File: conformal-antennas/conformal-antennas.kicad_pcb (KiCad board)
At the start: 2 copper layers, 153.9 x 117.1 mm, 1 part, among them J1 Conn_Coaxial

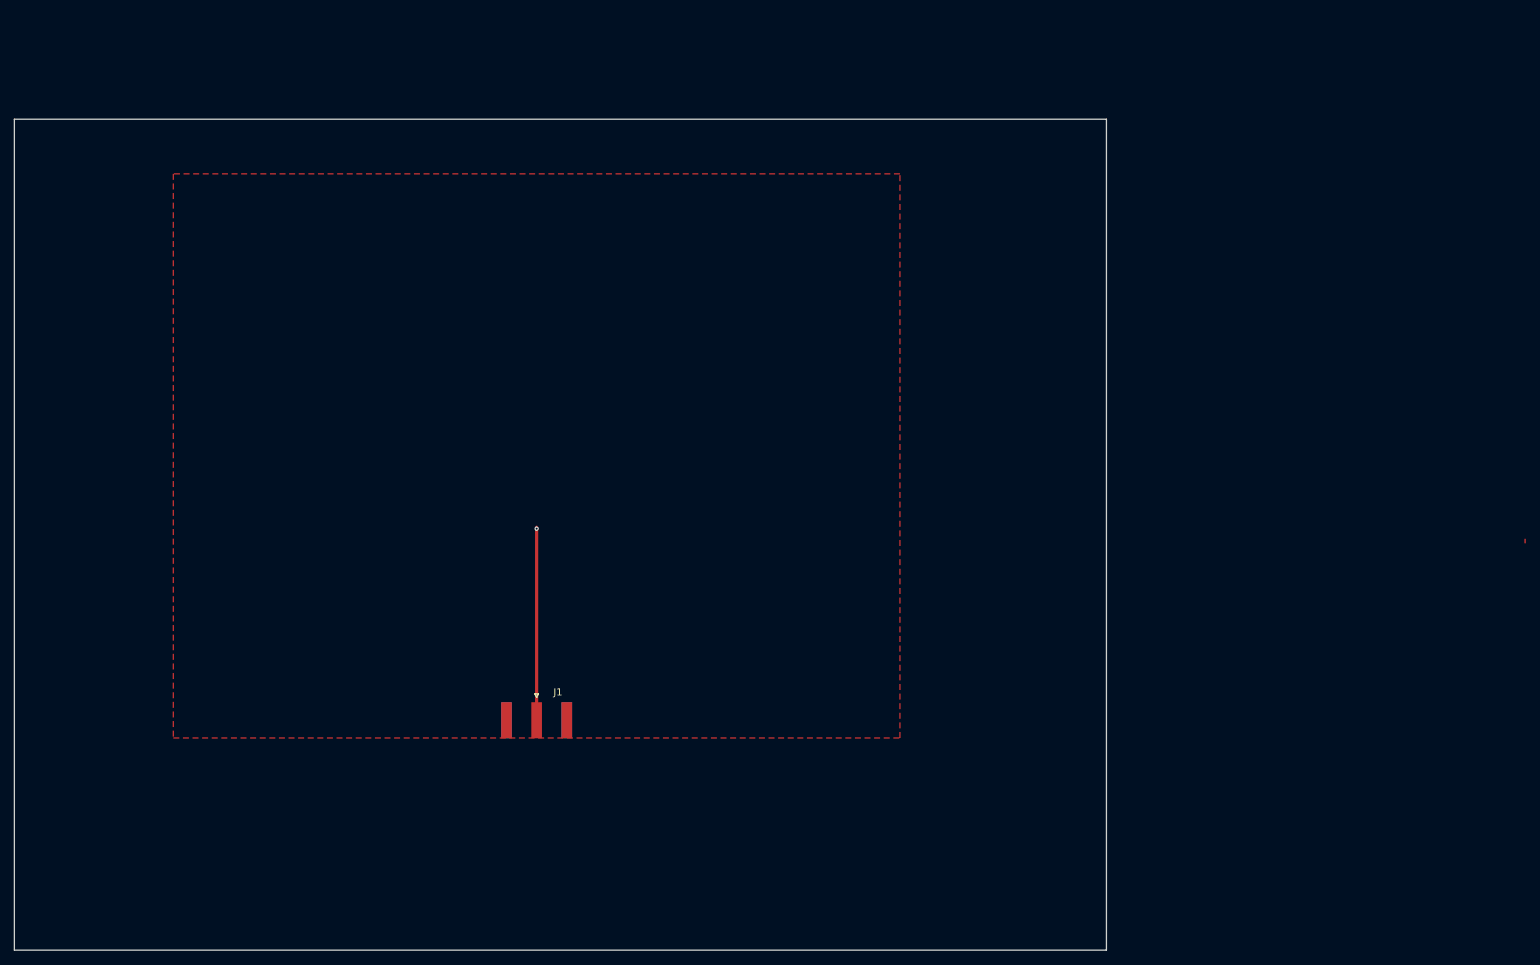
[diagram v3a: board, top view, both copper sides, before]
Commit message: Resized signal trace and added ground plane
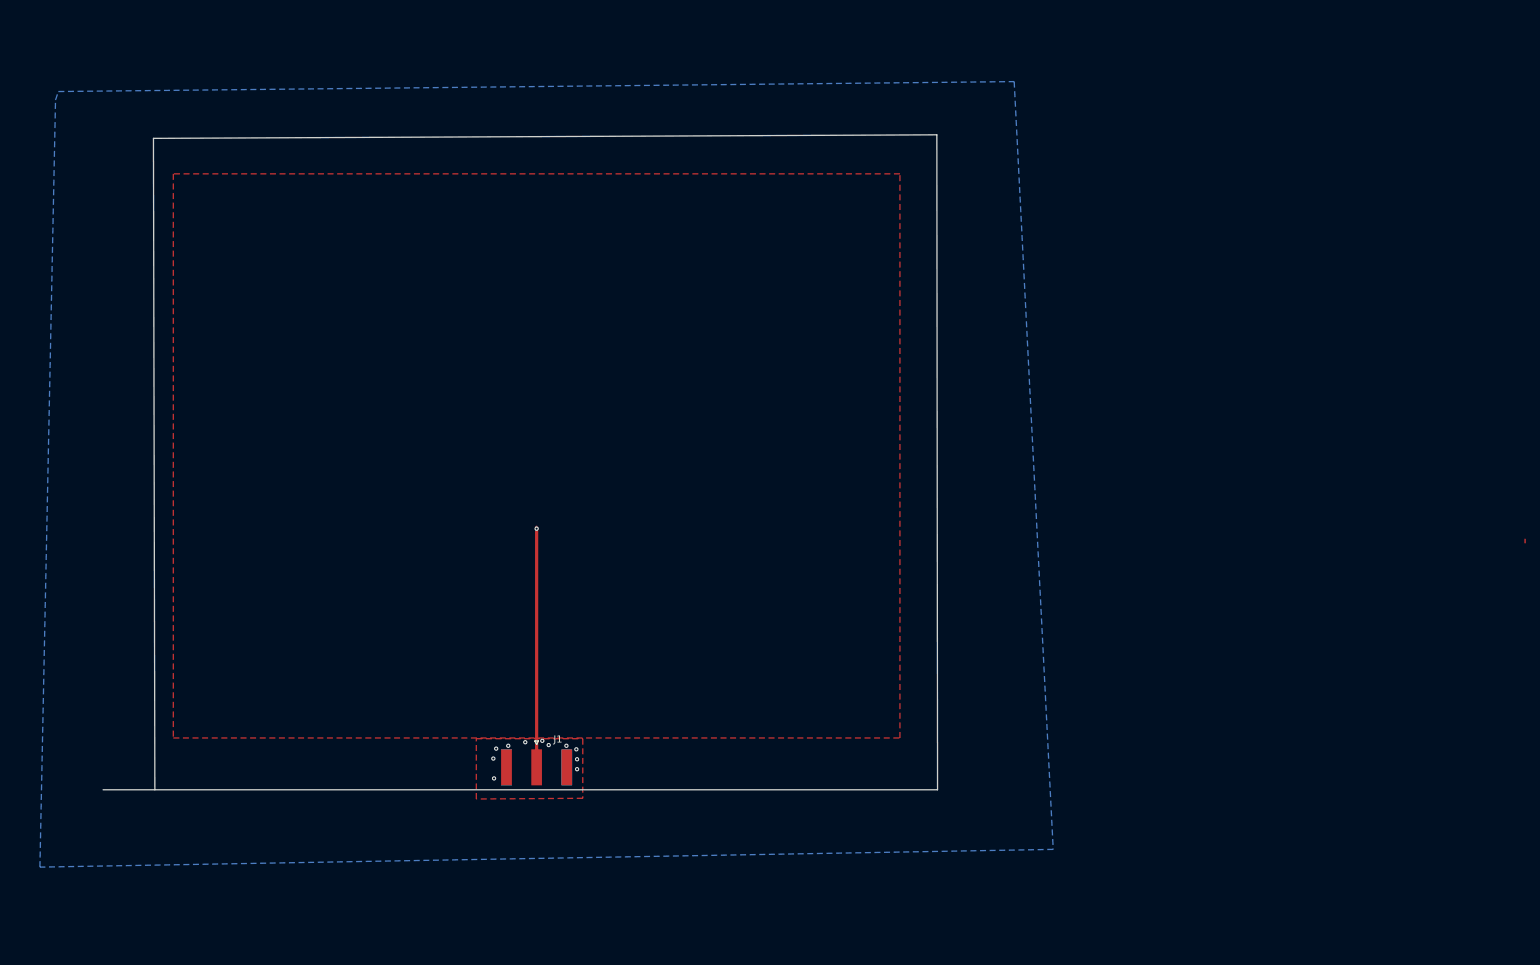
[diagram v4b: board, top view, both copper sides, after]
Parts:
- moved J1 6.64 mm to (108.2, 150.6)
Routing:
- net /Signal: track 27.2 -> 32.1 mm
- net GND: vias 0 -> 11
- added copper zone on B.Cu, net GND
- added copper zone on F.Cu, net GND
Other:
- board size 153.9 x 117.1 mm -> 117.6 x 92.3 mm
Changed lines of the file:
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@@
 	(footprint "Connector_Coaxial:SMA_Amphenol_132289_EdgeMount"
 		(layer "F.Cu")
-		(at 108.2 144 -90)
+		(at 108.2 150.6375 -90)
 		(descr "https://www.amphenolrf.com/library/download/link/link_id/595984/parent/132289/")
 		(tags "SMA")
@@
 		)
 	)
-	(gr_rect
-		(start 34.6 59.3)
-		(end 188.5 176.4)
+	(gr_line
+		(start 164.6 61.5)
+		(end 164.7 153.8)
 		(stroke
 			(width 0.05)
 			(type default)
 		)
-		(fill no)
+		(layer "Edge.Cuts")
+	)
+	(gr_line
+		(start 54.4 153.8)
+		(end 54.2 62)
+		(stroke
+			(width 0.05)
+			(type default)
+		)
+		(layer "Edge.Cuts")
+	)
+	(gr_line
+		(start 54.2 62)
+		(end 164.6 61.5)
+		(stroke
+			(width 0.05)
+			(type default)
+		)
+		(layer "Edge.Cuts")
+	)
+	(gr_line
+		(start 164.7 153.8)
+		(end 47.1 153.8)
+		(stroke
+			(width 0.05)
+			(type default)
+		)
 		(layer "Edge.Cuts")
 	)
@@
 		(net 0)
 	)
+	(via
+		(at 102.1 149.4)
+		(size 0.6)
+		(drill 0.3)
+		(layers "F.Cu" "B.Cu")
+		(free yes)
+		(net 1)
+	)
+	(via
+		(at 112.4 147.6)
+		(size 0.6)
+		(drill 0.3)
+		(layers "F.Cu" "B.Cu")
+		(free yes)
+		(net 1)
+	)
+	(via
+		(at 113.9 150.9)
+		(size 0.6)
+		(drill 0.3)
+		(layers "F.Cu" "B.Cu")
+		(free yes)
+		(net 1)
+	)
+	(via
+		(at 106.6 147.1)
+		(size 0.6)
+		(drill 0.3)
+		(layers "F.Cu" "B.Cu")
+		(free yes)
+		(net 1)
+	)
+	(via
+		(at 104.2 147.6)
+		(size 0.6)
+		(drill 0.3)
+		(layers "F.Cu" "B.Cu")
+		(free yes)
+		(net 1)
+	)
+	(via
+		(at 113.9 149.5)
+		(size 0.6)
+		(drill 0.3)
+		(layers "F.Cu" "B.Cu")
+		(free yes)
+		(net 1)
+	)
+	(via
+		(at 102.2 152.2)
+		(size 0.6)
+		(drill 0.3)
+		(layers "F.Cu" "B.Cu")
+		(free yes)
+		(net 1)
+	)
+	(via
+		(at 113.8 148.1)
+		(size 0.6)
+		(drill 0.3)
+		(layers "F.Cu" "B.Cu")
+		(free yes)
+		(net 1)
+	)
+	(via
+		(at 109 146.9)
+		(size 0.6)
+		(drill 0.3)
+		(layers "F.Cu" "B.Cu")
+		(free yes)
+		(net 1)
+	)
+	(via
+		(at 109.9 147.5)
+		(size 0.6)
+		(drill 0.3)
+		(layers "F.Cu" "B.Cu")
+		(free yes)
+		(net 1)
+	)
+	(via
+		(at 102.5 148)
+		(size 0.6)
+		(drill 0.3)
+		(layers "F.Cu" "B.Cu")
+		(free yes)
+		(net 1)
+	)
 	(segment
-		(start 108.2 144)
-		(end 108.2 117)
+		(start 108.2 117)
+		(end 108.2 148.874)
 		(width 0.45)
 		(layer "F.Cu")
@@
 			)
 		)
+	)
+	(zone
+		(net 1)
+		(net_name "GND")
+		(layer "F.Cu")
+		(hatch edge 0.5)
+		(priority 2)
+		(connect_pads yes
+			(clearance 0.5)
+		)
+		(min_thickness 0.25)
+		(filled_areas_thickness no)
+		(fill yes
+			(thermal_gap 0.5)
+			(thermal_bridge_width 0.5)
+		)
+		(polygon
+			(pts
+				(xy 114.7 146.6) (xy 114.7 155) (xy 99.7 155.1) (xy 99.7 146.6)
+			)
+		)
+	)
+	(zone
+		(net 1)
+		(net_name "GND")
+		(layer "B.Cu")
+		(hatch edge 0.5)
+		(priority 1)
+		(connect_pads yes
+			(clearance 0.5)
+		)
+		(min_thickness 0.25)
+		(filled_areas_thickness no)
+		(fill yes
+			(thermal_gap 0.5)
+			(thermal_bridge_width 0.5)
+		)
+		(polygon
+			(pts
+				(xy 40.8 55.4) (xy 175.5 54) (xy 181 162.2) (xy 38.2 164.7) (xy 40.4 56.6)
+			)
+		)
